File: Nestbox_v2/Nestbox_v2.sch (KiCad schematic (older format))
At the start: 0 parts

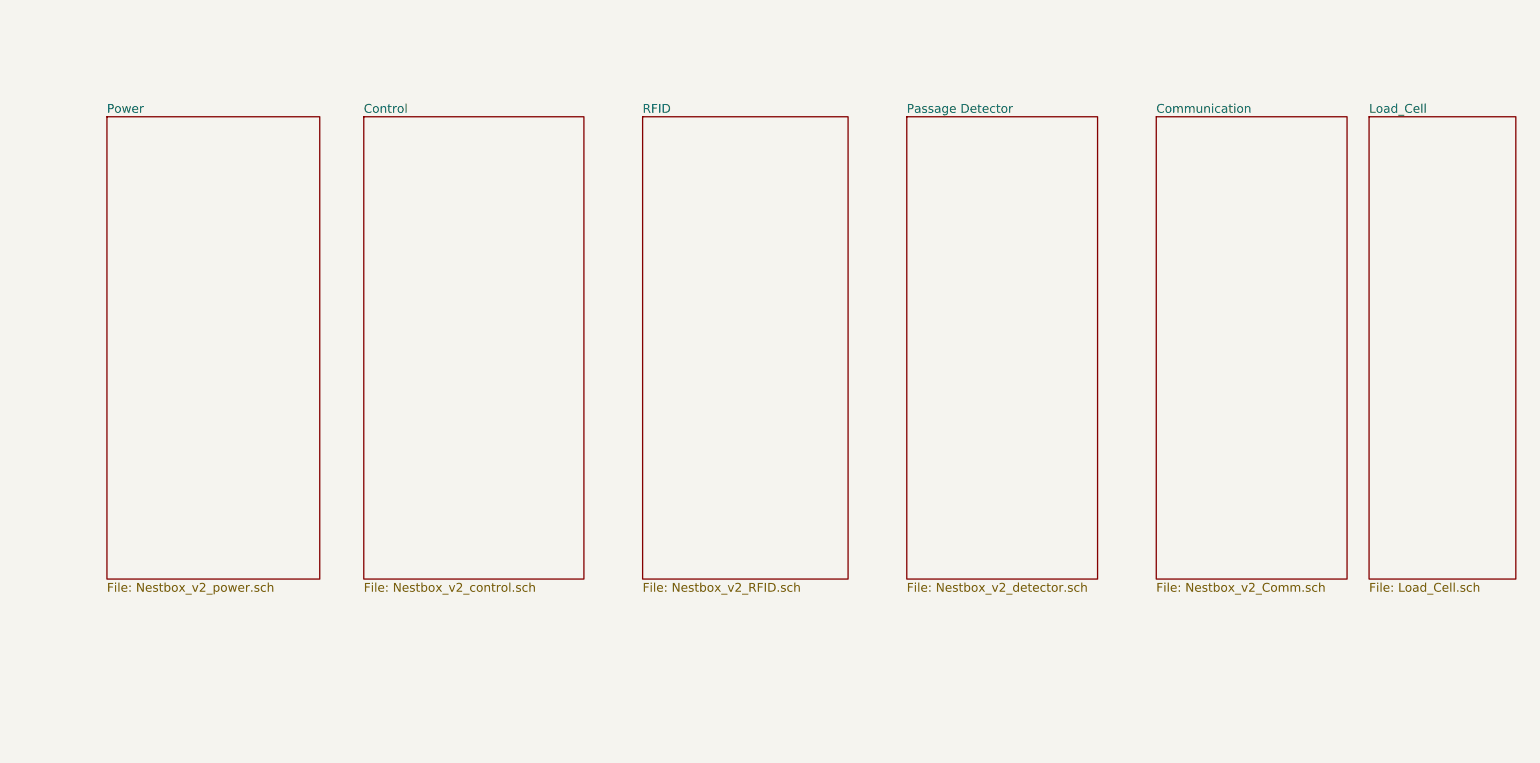
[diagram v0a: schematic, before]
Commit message: created V2 MLX breakout board
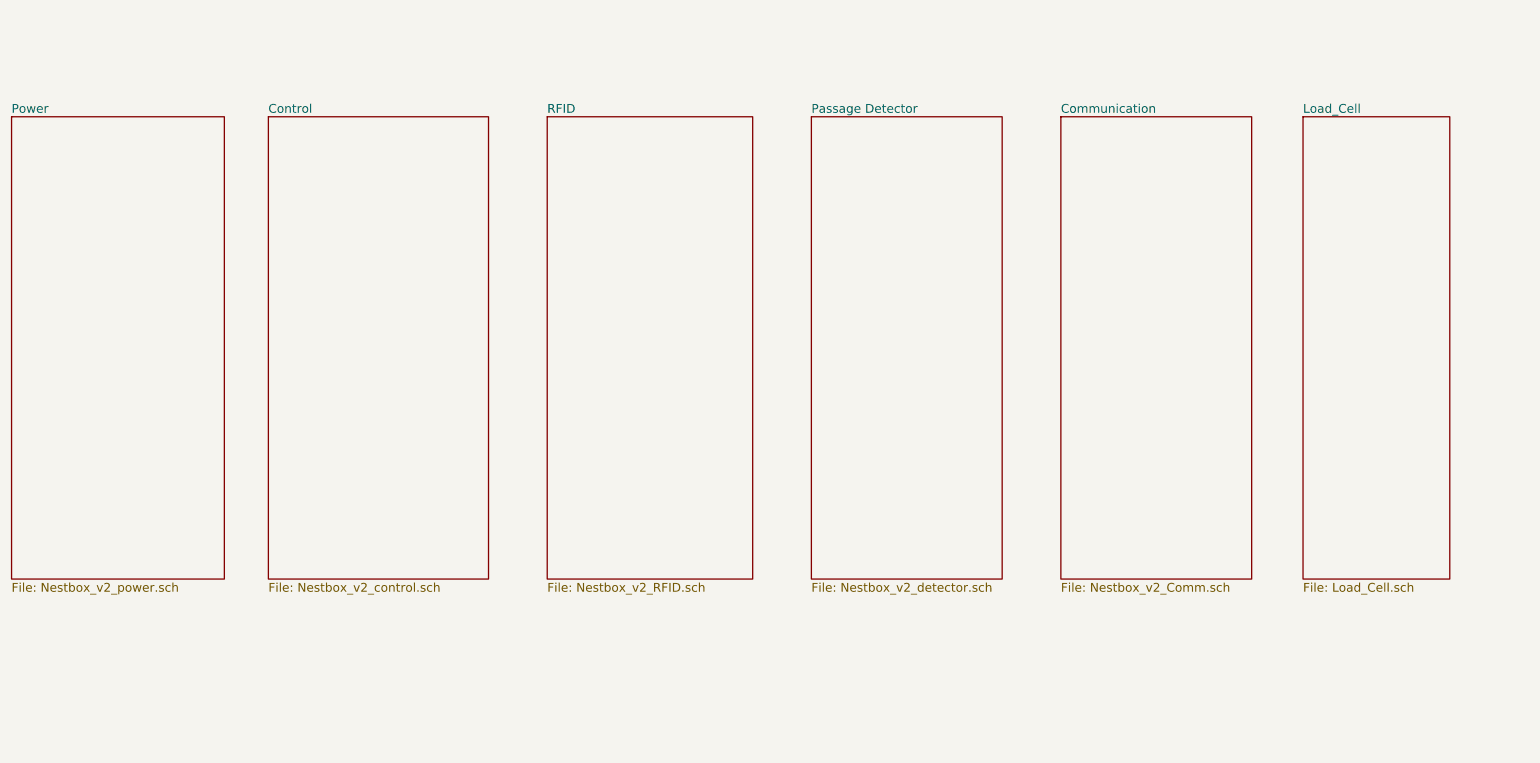
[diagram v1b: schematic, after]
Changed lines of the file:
@@
 $EndDescr
 $Sheet
-S 1450 1750 1450 3150
+S 800  1750 1450 3150
 U 59EF7EEA
 F0 "Power" 60
@@
 $EndSheet
 $Sheet
-S 3200 1750 1500 3150
+S 2550 1750 1500 3150
 U 59EF7F04
 F0 "Control" 60
@@
 $EndSheet
 $Sheet
-S 5100 1750 1400 3150
+S 4450 1750 1400 3150
 U 59EF7F28
 F0 "RFID" 60
@@
 $EndSheet
 $Sheet
-S 6900 1750 1300 3150
+S 6250 1750 1300 3150
 U 59EF7F41
 F0 "Passage Detector" 60
@@
 $EndSheet
 $Sheet
-S 8600 1750 1300 3150
+S 7950 1750 1300 3150
 U 59F63D06
 F0 "Communication" 60
@@
 $EndSheet
 $Sheet
-S 10050 1750 1000 3150
+S 9600 1750 1000 3150
 U 5AF72069
 F0 "Load_Cell" 60

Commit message: restructured top level sheet with hierarchical labels, assigned most GPIOs
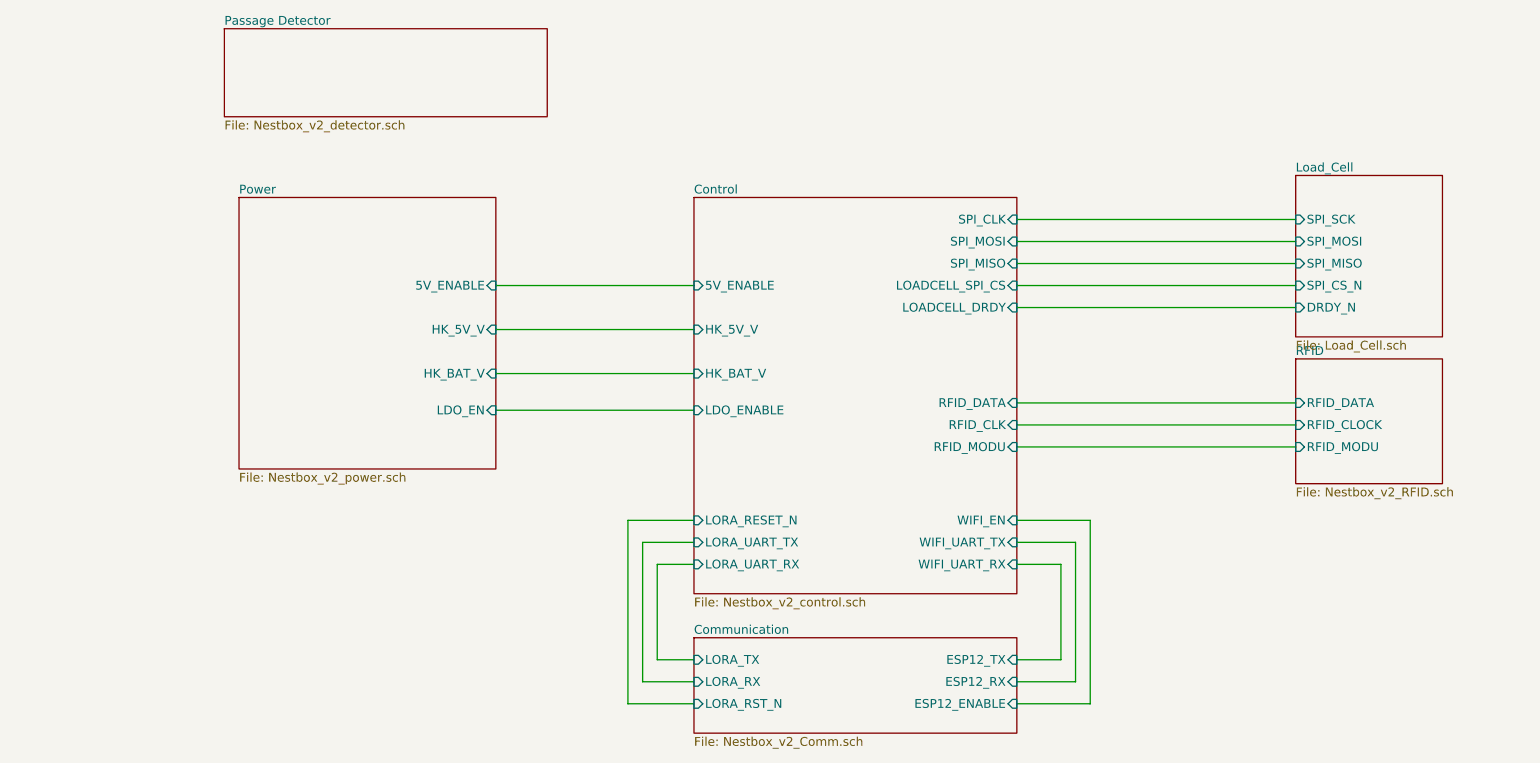
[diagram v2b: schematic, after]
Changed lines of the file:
@@
 LIBS:SeeedOPL-Transistor-2016
 LIBS:Nestbox_v2-cache
-EELAYER 26 0
+EELAYER 25 0
 EELAYER END
 $Descr A4 11693 8268
@@
 $EndDescr
 $Sheet
-S 800  1750 1450 3150
+S 2350 2300 1750 1850
 U 59EF7EEA
 F0 "Power" 60
 F1 "Nestbox_v2_power.sch" 60
+F2 "5V_ENABLE" I R 4100 2900 60
+F3 "HK_5V_V" I R 4100 3200 60
+F4 "HK_BAT_V" I R 4100 3500 60
+F5 "LDO_EN" I R 4100 3750 60
 $EndSheet
 $Sheet
-S 2550 1750 1500 3150
+S 5450 2300 2200 2700
 U 59EF7F04
 F0 "Control" 60
 F1 "Nestbox_v2_control.sch" 60
+F2 "SPI_MISO" I R 7650 2750 60
+F3 "SPI_MOSI" I R 7650 2600 60
+F4 "LOADCELL_SPI_CS" I R 7650 2900 60
+F5 "SPI_CLK" I R 7650 2450 60
+F6 "LOADCELL_DRDY" I R 7650 3050 60
+F7 "RFID_DATA" I R 7650 3700 60
+F8 "RFID_MODU" I R 7650 4000 60
+F9 "RFID_CLK" I R 7650 3850 60
+F10 "HK_5V_V" I L 5450 3200 60
+F11 "HK_BAT_V" I L 5450 3500 60
+F12 "5V_ENABLE" I L 5450 2900 60
+F13 "LDO_ENABLE" I L 5450 3750 60
+F14 "WIFI_UART_TX" I R 7650 4650 60
+F15 "WIFI_UART_RX" I R 7650 4800 60
+F16 "LORA_RESET_N" I L 5450 4500 60
+F17 "WIFI_EN" I R 7650 4500 60
+F18 "LORA_UART_TX" I L 5450 4650 60
+F19 "LORA_UART_RX" I L 5450 4800 60
 $EndSheet
 $Sheet
-S 4450 1750 1400 3150
+S 9550 3400 1000 850
 U 59EF7F28
 F0 "RFID" 60
 F1 "Nestbox_v2_RFID.sch" 60
+F2 "RFID_DATA" I L 9550 3700 60
+F3 "RFID_CLOCK" I L 9550 3850 60
+F4 "RFID_MODU" I L 9550 4000 60
 $EndSheet
 $Sheet
-S 6250 1750 1300 3150
+S 2250 1150 2200 600
 U 59EF7F41
 F0 "Passage Detector" 60
@@
 $EndSheet
 $Sheet
-S 7950 1750 1300 3150
+S 5450 5300 2200 650
 U 59F63D06
 F0 "Communication" 60
 F1 "Nestbox_v2_Comm.sch" 60
+F2 "ESP12_TX" I R 7650 5450 60
+F3 "ESP12_RX" I R 7650 5600 60
+F4 "ESP12_ENABLE" I R 7650 5750 60
+F5 "LORA_RX" I L 5450 5600 60
+F6 "LORA_TX" I L 5450 5450 60
+F7 "LORA_RST_N" I L 5450 5750 60
 $EndSheet
 $Sheet
-S 9600 1750 1000 3150
+S 9550 2150 1000 1100
 U 5AF72069
 F0 "Load_Cell" 60
 F1 "Load_Cell.sch" 60
+F2 "SPI_SCK" I L 9550 2450 60
+F3 "SPI_MOSI" I L 9550 2600 60
+F4 "SPI_MISO" I L 9550 2750 60
+F5 "SPI_CS_N" I L 9550 2900 60
+F6 "DRDY_N" I L 9550 3050 60
 $EndSheet
+Wire Wire Line
+	7650 3700 9550 3700
+Wire Wire Line
+	7650 3850 9550 3850
+Wire Wire Line
+	7650 4000 9550 4000
+Wire Wire Line
+	5450 2900 4100 2900
+Wire Wire Line
+	4100 3200 5450 3200
+Wire Wire Line
+	5450 3500 4100 3500
+Wire Wire Line
+	4100 3750 5450 3750
+Wire Wire Line
+	7650 4500 8150 4500
+Wire Wire Line
+	8150 4500 8150 5750
+Wire Wire Line
+	8150 5750 7650 5750
+Wire Wire Line
+	7650 4650 8050 4650
+Wire Wire Line
+	8050 4650 8050 5600
+Wire Wire Line
+	8050 5600 7650 5600
+Wire Wire Line
+	7650 4800 7950 4800
+Wire Wire Line
+	7950 4800 7950 5450
+Wire Wire Line
+	7950 5450 7650 5450
+Wire Wire Line
+	5450 4800 5200 4800
+Wire Wire Line
+	5200 4800 5200 5450
+Wire Wire Line
+	5200 5450 5450 5450
+Wire Wire Line
+	5450 4650 5100 4650
+Wire Wire Line
+	5100 4650 5100 5600
+Wire Wire Line
+	5100 5600 5450 5600
+Wire Wire Line
+	5450 4500 5000 4500
+Wire Wire Line
+	5000 4500 5000 5750
+Wire Wire Line
+	5000 5750 5450 5750
+Wire Wire Line
+	9550 2450 7650 2450
+Wire Wire Line
+	7650 2600 9550 2600
+Wire Wire Line
+	9550 2750 7650 2750
+Wire Wire Line
+	9550 2900 7650 2900
+Wire Wire Line
+	9550 3050 7650 3050
 $EndSCHEMATC

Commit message: finished power supply schematics
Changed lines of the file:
@@
 F1 "Nestbox_v2_power.sch" 60
 F2 "5V_ENABLE" I R 4100 2900 60
-F3 "HK_5V_V" I R 4100 3200 60
-F4 "HK_BAT_V" I R 4100 3500 60
-F5 "LDO_EN" I R 4100 3750 60
+F3 "HK_BAT_V" I R 4100 3500 60
+F4 "LDO_EN" I R 4100 3750 60
+F5 "BAT_TEST_ENABLE" I R 4100 3350 60
+F6 "5V_PG" I R 4100 3050 60
 $EndSheet
 $Sheet
@@
 F6 "LOADCELL_DRDY" I R 7650 3050 60
 F7 "RFID_DATA" I R 7650 3700 60
-F8 "RFID_MODU" I R 7650 4000 60
-F9 "RFID_CLK" I R 7650 3850 60
-F10 "HK_5V_V" I L 5450 3200 60
-F11 "HK_BAT_V" I L 5450 3500 60
-F12 "5V_ENABLE" I L 5450 2900 60
-F13 "LDO_ENABLE" I L 5450 3750 60
-F14 "WIFI_UART_TX" I R 7650 4650 60
-F15 "WIFI_UART_RX" I R 7650 4800 60
-F16 "LORA_RESET_N" I L 5450 4500 60
-F17 "WIFI_EN" I R 7650 4500 60
-F18 "LORA_UART_TX" I L 5450 4650 60
-F19 "LORA_UART_RX" I L 5450 4800 60
-$EndSheet
-$Sheet
-S 9550 3400 1000 850
-U 59EF7F28
-F0 "RFID" 60
-F1 "Nestbox_v2_RFID.sch" 60
-F2 "RFID_DATA" I L 9550 3700 60
-F3 "RFID_CLOCK" I L 9550 3850 60
-F4 "RFID_MODU" I L 9550 4000 60
+F8 "RFID_CLK" I R 7650 3850 60
+F9 "HK_5V_V" I L 5450 3050 60
+F10 "HK_BAT_V" I L 5450 3500 60
+F11 "5V_ENABLE" I L 5450 2900 60
+F12 "LDO_ENABLE" I L 5450 3750 60
+F13 "WIFI_UART_TX" I R 7650 4650 60
+F14 "WIFI_UART_RX" I R 7650 4800 60
+F15 "LORA_RESET_N" I L 5450 4500 60
+F16 "WIFI_EN" I R 7650 4500 60
+F17 "LORA_UART_TX" I L 5450 4650 60
+F18 "LORA_UART_RX" I L 5450 4800 60
+F19 "LOADCELL_EXC_A_P" I R 7650 3200 60
+F20 "LOADCELL_EXC_A_N" I R 7650 3300 60
+F21 "LOADCELL_EXC_B_P" I R 7650 3400 60
+F22 "LOADCELL_EXC_B_N" I R 7650 3500 60
+F23 "RFID_SLEEP_N" I R 7650 4000 60
+F24 "BAT_TEST_ENABLE" I L 5450 3350 60
 $EndSheet
 $Sheet
@@
 F5 "SPI_CS_N" I L 9550 2900 60
 F6 "DRDY_N" I L 9550 3050 60
+F7 "EXC_A_P" I R 10550 2450 60
+F8 "EXC_A_N" I R 10550 2600 60
+F9 "EXC_B_N" I R 10550 3050 60
+F10 "EXC_B_P" I R 10550 2900 60
 $EndSheet
 Wire Wire Line
-	7650 3700 9550 3700
+	7650 3700 9550 3950
 Wire Wire Line
-	7650 3850 9550 3850
+	7650 3850 9550 4100
 Wire Wire Line
-	7650 4000 9550 4000
+	7650 4000 9550 4250
 Wire Wire Line
 	5450 2900 4100 2900
-Wire Wire Line
-	4100 3200 5450 3200
 Wire Wire Line
 	5450 3500 4100 3500
@@
 Wire Wire Line
 	9550 3050 7650 3050
+$Sheet
+S 9550 3650 1000 850
+U 59EF7F28
+F0 "RFID" 60
+F1 "Nestbox_v2_RFID.sch" 60
+F2 "RFID_DATA" I L 9550 3950 60
+F3 "RFID_CLOCK" I L 9550 4100 60
+F4 "RFID_SLEEP_N" I L 9550 4250 60
+$EndSheet
+Wire Wire Line
+	5450 3050 4100 3050
+Wire Wire Line
+	5450 3350 4100 3350
+Wire Wire Line
+	7650 3200 8650 3200
+Wire Wire Line
+	8650 3200 8650 2000
+Wire Wire Line
+	8650 2000 10750 2000
+Wire Wire Line
+	10750 2000 10750 2450
+Wire Wire Line
+	10750 2450 10550 2450
+Wire Wire Line
+	7650 3300 8800 3300
+Wire Wire Line
+	8800 3300 8800 1900
+Wire Wire Line
+	8800 1900 10850 1900
+Wire Wire Line
+	10850 1900 10850 2600
+Wire Wire Line
+	10850 2600 10550 2600
+Wire Wire Line
+	7650 3400 10750 3400
+Wire Wire Line
+	10750 3400 10750 2900
+Wire Wire Line
+	10750 2900 10550 2900
+Wire Wire Line
+	7650 3500 10850 3500
+Wire Wire Line
+	10850 3500 10850 3050
+Wire Wire Line
+	10850 3050 10550 3050
 $EndSCHEMATC

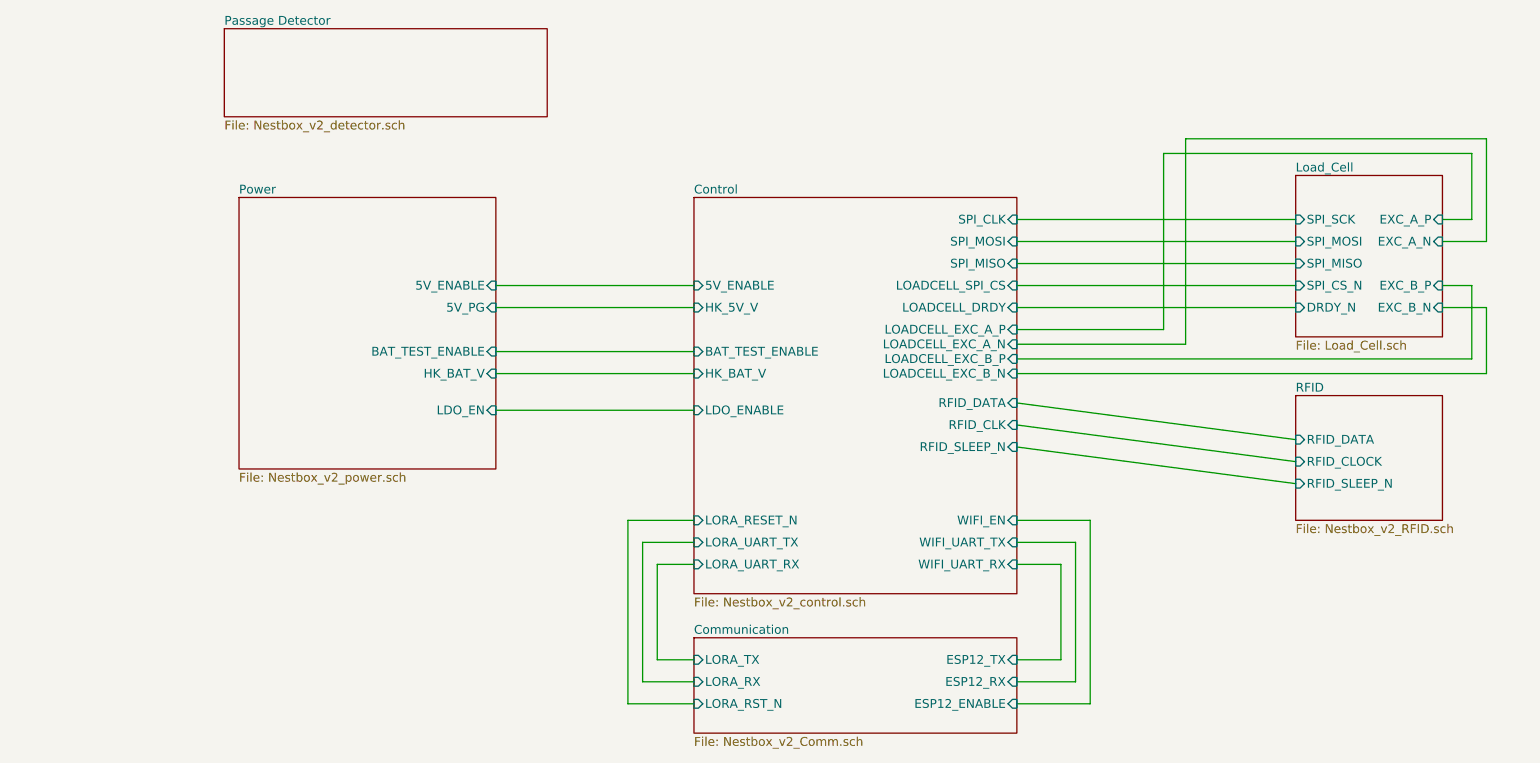
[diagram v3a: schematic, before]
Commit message: added PIR and lightbarrier headers
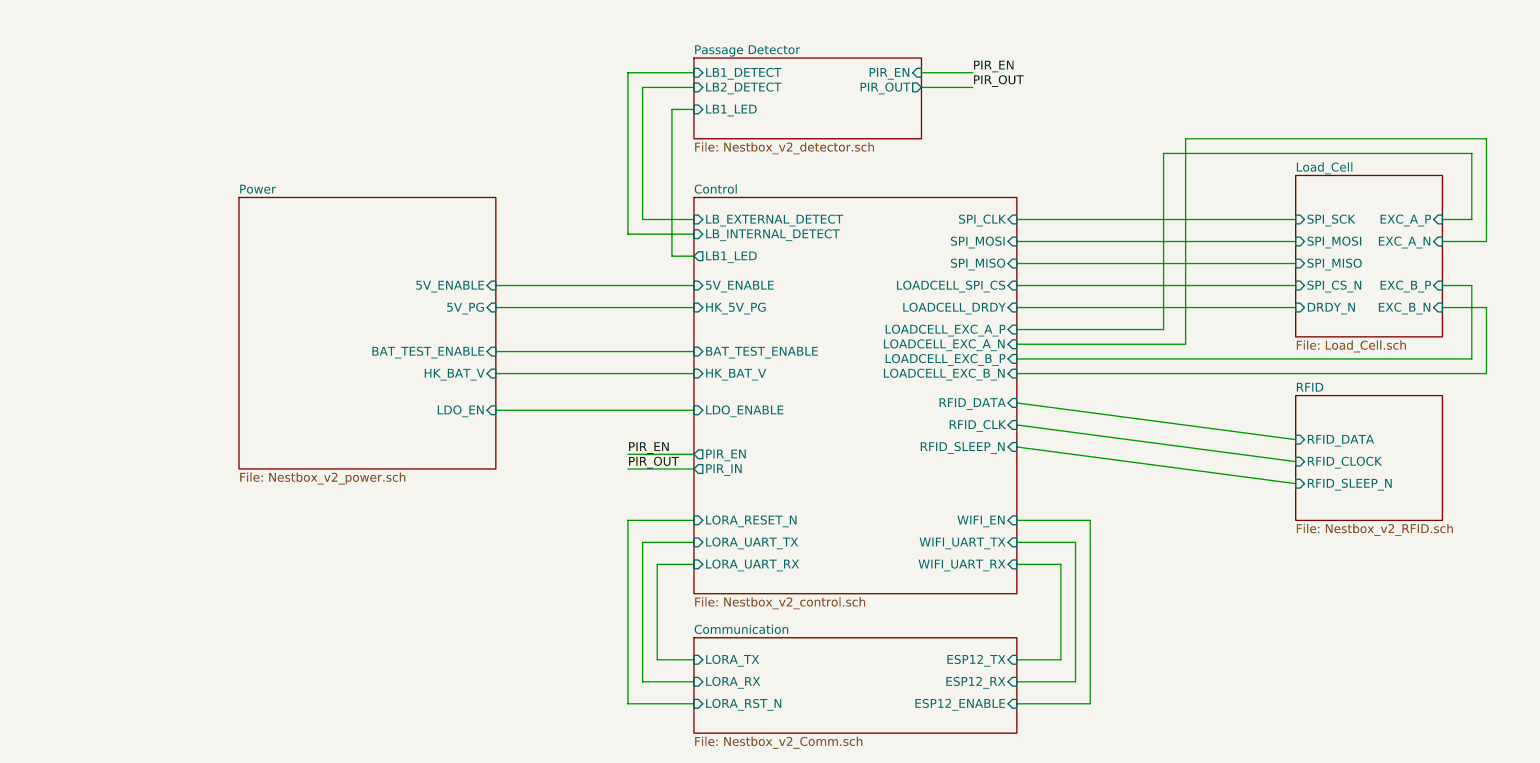
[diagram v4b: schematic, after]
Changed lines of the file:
@@
 F7 "RFID_DATA" I R 7650 3700 60
 F8 "RFID_CLK" I R 7650 3850 60
-F9 "HK_5V_V" I L 5450 3050 60
-F10 "HK_BAT_V" I L 5450 3500 60
-F11 "5V_ENABLE" I L 5450 2900 60
-F12 "LDO_ENABLE" I L 5450 3750 60
-F13 "WIFI_UART_TX" I R 7650 4650 60
-F14 "WIFI_UART_RX" I R 7650 4800 60
-F15 "LORA_RESET_N" I L 5450 4500 60
-F16 "WIFI_EN" I R 7650 4500 60
-F17 "LORA_UART_TX" I L 5450 4650 60
-F18 "LORA_UART_RX" I L 5450 4800 60
-F19 "LOADCELL_EXC_A_P" I R 7650 3200 60
-F20 "LOADCELL_EXC_A_N" I R 7650 3300 60
-F21 "LOADCELL_EXC_B_P" I R 7650 3400 60
-F22 "LOADCELL_EXC_B_N" I R 7650 3500 60
-F23 "RFID_SLEEP_N" I R 7650 4000 60
-F24 "BAT_TEST_ENABLE" I L 5450 3350 60
-$EndSheet
-$Sheet
-S 2250 1150 2200 600
+F9 "HK_BAT_V" I L 5450 3500 60
+F10 "5V_ENABLE" I L 5450 2900 60
+F11 "LDO_ENABLE" I L 5450 3750 60
+F12 "WIFI_UART_TX" I R 7650 4650 60
+F13 "WIFI_UART_RX" I R 7650 4800 60
+F14 "LORA_RESET_N" I L 5450 4500 60
+F15 "WIFI_EN" I R 7650 4500 60
+F16 "LORA_UART_TX" I L 5450 4650 60
+F17 "LORA_UART_RX" I L 5450 4800 60
+F18 "LOADCELL_EXC_A_P" I R 7650 3200 60
+F19 "LOADCELL_EXC_A_N" I R 7650 3300 60
+F20 "LOADCELL_EXC_B_P" I R 7650 3400 60
+F21 "LOADCELL_EXC_B_N" I R 7650 3500 60
+F22 "RFID_SLEEP_N" I R 7650 4000 60
+F23 "BAT_TEST_ENABLE" I L 5450 3350 60
+F24 "HK_5V_PG" I L 5450 3050 60
+F25 "LB_INTERNAL_DETECT" I L 5450 2550 60
+F26 "LB_EXTERNAL_DETECT" I L 5450 2450 60
+F27 "LB1_LED" O L 5450 2700 60
+F28 "PIR_EN" O L 5450 4050 60
+F29 "PIR_IN" O L 5450 4150 60
+$EndSheet
+$Sheet
+S 5450 1350 1550 550
 U 59EF7F41
 F0 "Passage Detector" 60
 F1 "Nestbox_v2_detector.sch" 60
+F2 "LB1_DETECT" I L 5450 1450 60
+F3 "LB1_LED" I L 5450 1700 60
+F4 "LB2_DETECT" I L 5450 1550 60
+F5 "PIR_EN" I R 7000 1450 60
+F6 "PIR_OUT" O R 7000 1550 60
 $EndSheet
 $Sheet
@@
 Wire Wire Line
 	10850 3050 10550 3050
+Wire Wire Line
+	5450 1450 5000 1450
+Wire Wire Line
+	5000 1450 5000 2550
+Wire Wire Line
+	5000 2550 5450 2550
+Wire Wire Line
+	5450 2450 5100 2450
+Wire Wire Line
+	5100 2450 5100 1550
+Wire Wire Line
+	5100 1550 5450 1550
+Wire Wire Line
+	5450 1700 5300 1700
+Wire Wire Line
+	5300 1700 5300 2700
+Wire Wire Line
+	5300 2700 5450 2700
+Wire Wire Line
+	5450 4050 5000 4050
+Wire Wire Line
+	5000 4150 5450 4150
+Wire Wire Line
+	7000 1450 7350 1450
+Wire Wire Line
+	7000 1550 7350 1550
+Text Label 7350 1450 0    60   ~ 0
+PIR_EN
+Text Label 7350 1550 0    60   ~ 0
+PIR_OUT
+Text Label 5000 4050 0    60   ~ 0
+PIR_EN
+Text Label 5000 4150 0    60   ~ 0
+PIR_OUT
 $EndSCHEMATC
